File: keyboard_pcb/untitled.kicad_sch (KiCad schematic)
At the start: 33 parts, among them J1 USB_C_Receptacle_USB2.0_16P, J2 Conn_01x02, SW1 Reset, U1 RP2040, U2 NCP1117-3.3_SOT223, U3 W25Q128JVS, Y1 Crystal_GND24

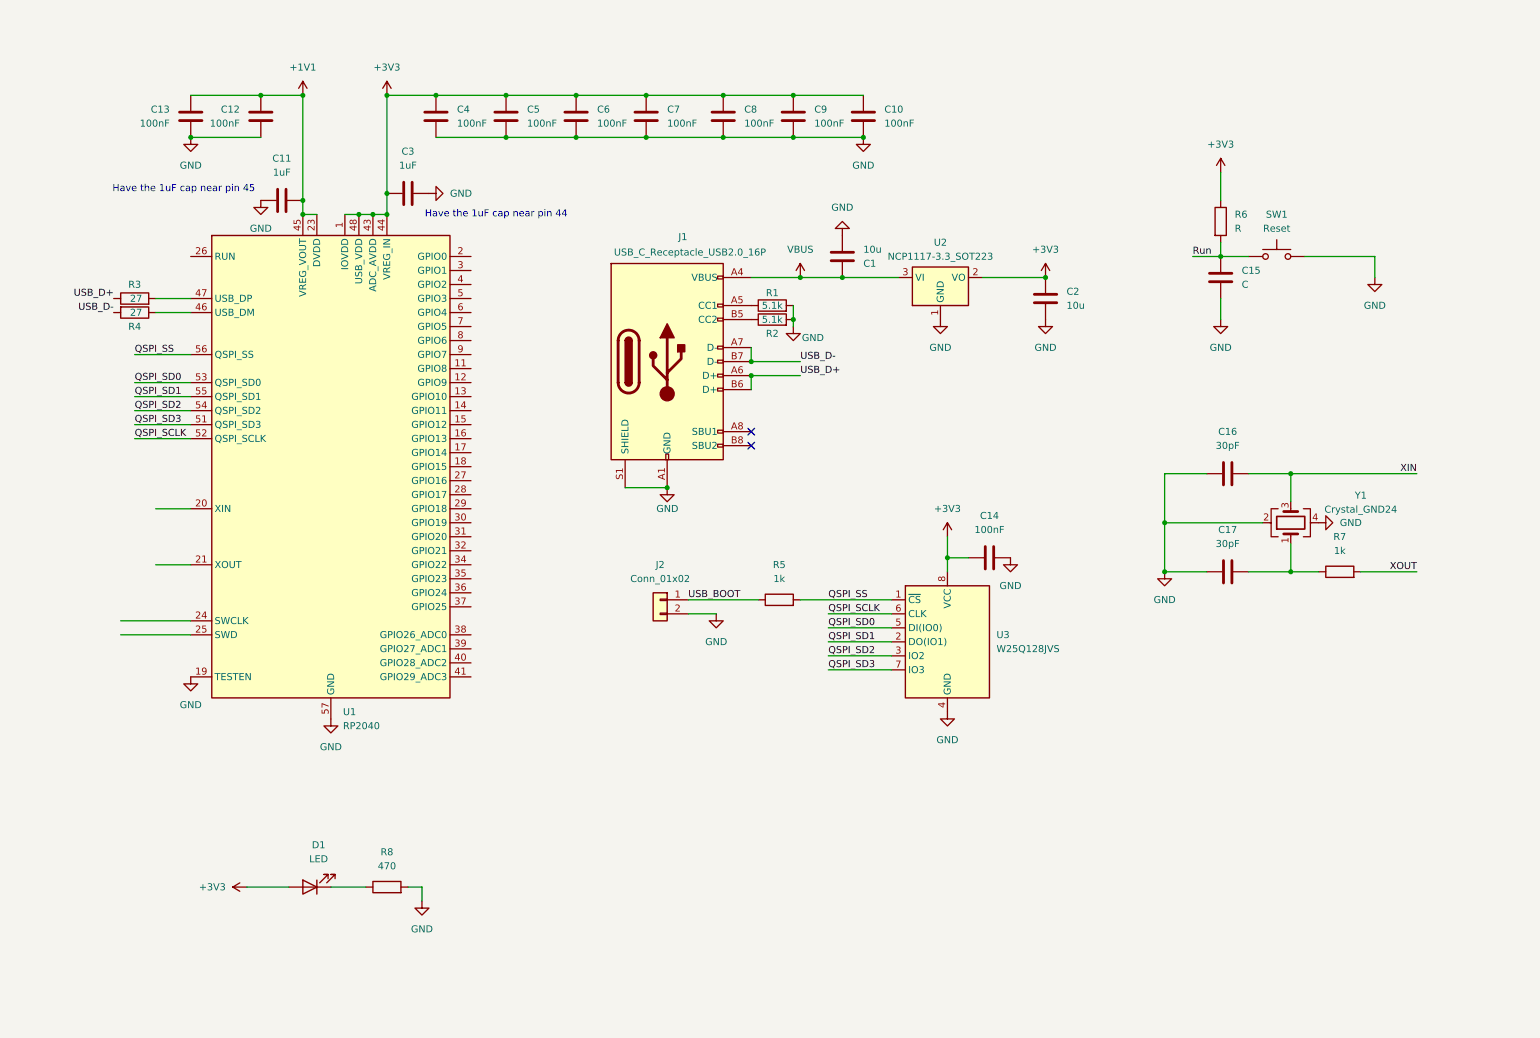
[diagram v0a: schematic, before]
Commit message: implemented matrix
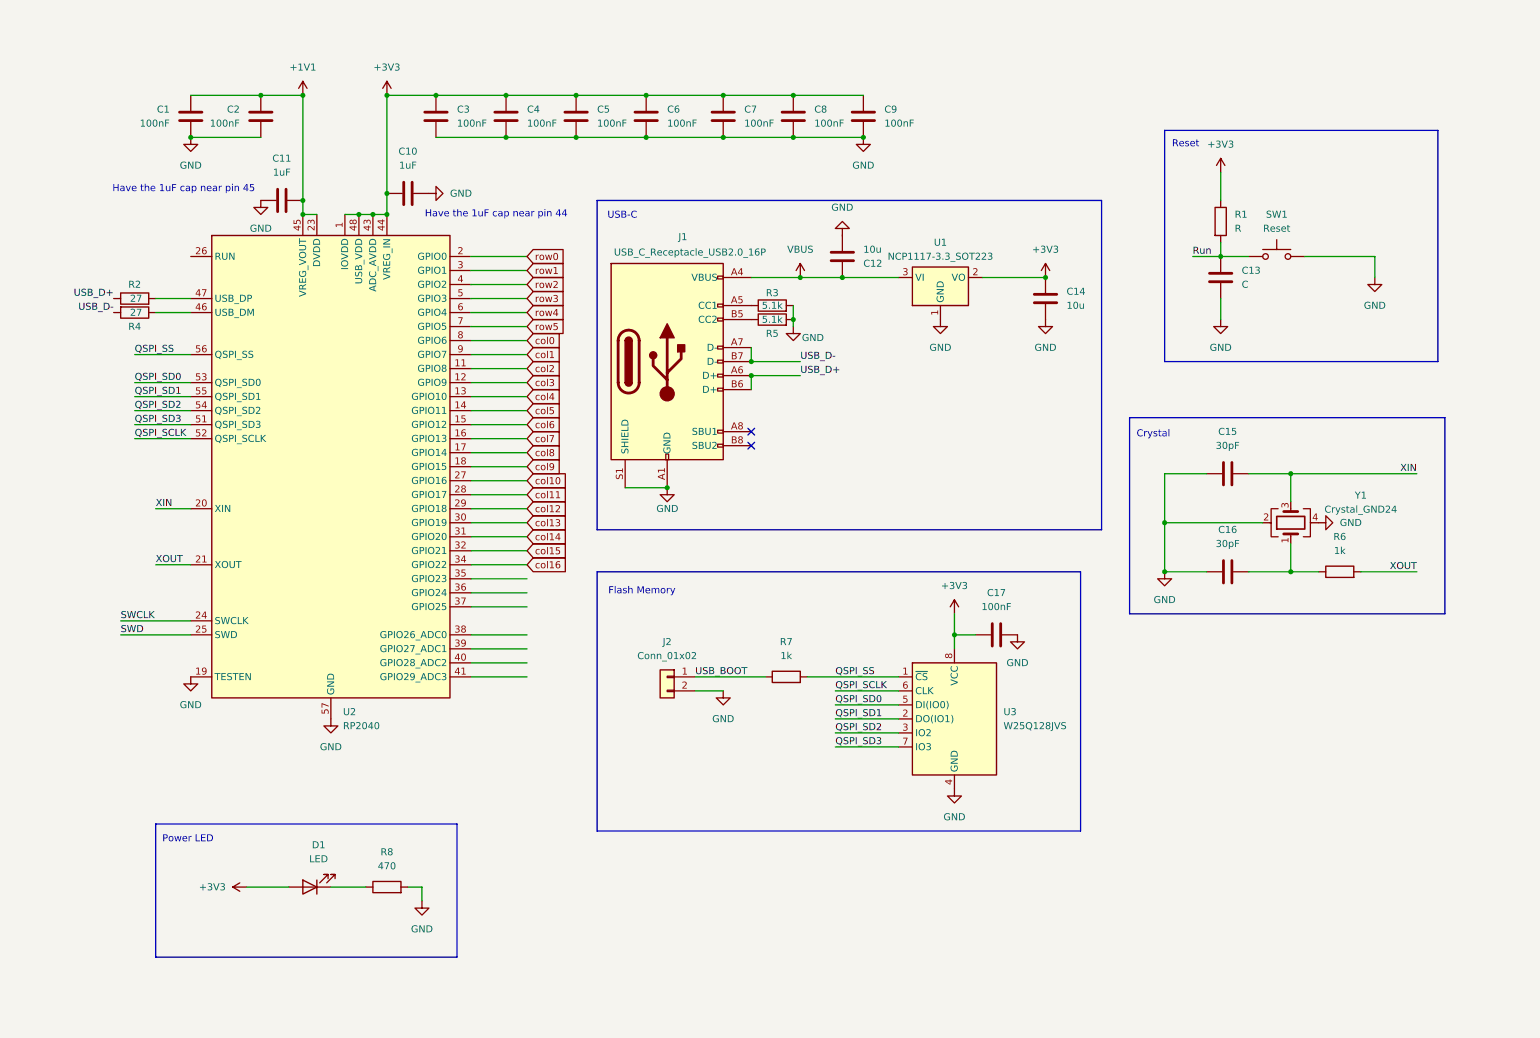
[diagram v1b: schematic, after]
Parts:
- renumbered C13 to C1, C3 to C10, C1 to C12, C15 to C13, C2 to C14, C16 to C15, C17 to C16, C14 to C17, C12 to C2, C4 to C3, C5 to C4, C6 to C5, C7 to C6, C8 to C7, C9 to C8, C10 to C9, R6 to R1, R3 to R2, R1 to R3, R2 to R5, R7 to R6, R5 to R7, U2 to U1, U1 to U2
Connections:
- net XIN: now also U2.20 (XIN)
- net XOUT: now also U2.21 (XOUT)
- net col2: now reaches U2.11 (GPIO8)
- net col3: now reaches U2.12 (GPIO9)
- net col4: now reaches U2.13 (GPIO10)
- net col5: now reaches U2.14 (GPIO11)
- net col6: now reaches U2.15 (GPIO12)
- net col7: now reaches U2.16 (GPIO13)
- net col8: now reaches U2.17 (GPIO14)
- net col9: now reaches U2.18 (GPIO15)
- net row0: now reaches U2.2 (GPIO0)
- net SWCLK: now reaches U2.24 (SWCLK)
- net SWD: now reaches U2.25 (SWD)
- net col10: now reaches U2.27 (GPIO16)
- net col11: now reaches U2.28 (GPIO17)
- net col12: now reaches U2.29 (GPIO18)
- net row1: now reaches U2.3 (GPIO1)
- net col13: now reaches U2.30 (GPIO19)
- net col14: now reaches U2.31 (GPIO20)
- net col15: now reaches U2.32 (GPIO21)
- net col16: now reaches U2.34 (GPIO22)
- net row2: now reaches U2.4 (GPIO2)
- net row3: now reaches U2.5 (GPIO3)
- net row4: now reaches U2.6 (GPIO4)
- net row5: now reaches U2.7 (GPIO5)
- net col0: now reaches U2.8 (GPIO6)
- net col1: now reaches U2.9 (GPIO7)
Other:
- note added: "Crystal"
- note added: "Flash Memory"
- note added: "Power LED"
- note added: "Reset"
- note added: "USB-C"
- moved on the sheet: C17, J2, R7, U3

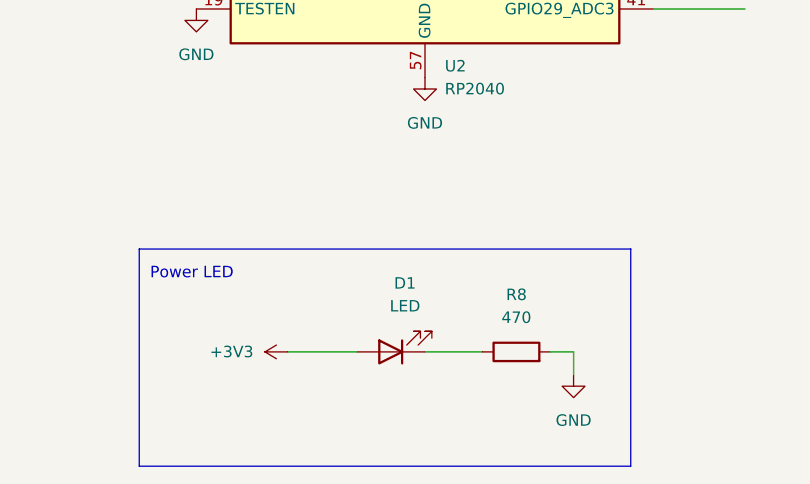
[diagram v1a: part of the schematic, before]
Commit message: implemented LEDs and switch and diode layout
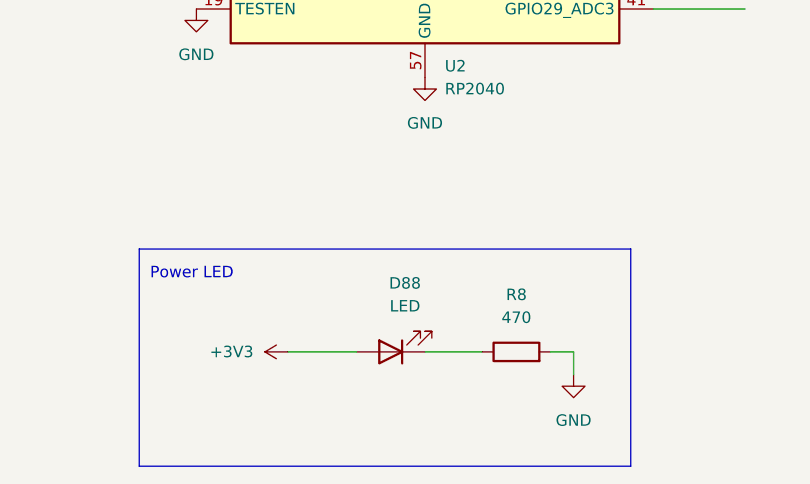
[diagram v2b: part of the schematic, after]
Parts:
- renumbered D1 to D88
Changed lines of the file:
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@@
 		(dnp no)
 		(fields_autoplaced yes)
-		(property "Reference" "D1"
+		(property "Reference" "D88"
 			(at 65.0875 163.83 0)
 			(effects
@@
 			(project ""
 				(path "/5a0b976f-d314-4fca-8ab0-732ea8a514fc/1c1519bd-c066-477c-a904-4026770e74a9"
-					(reference "D1")
+					(reference "D88")
 					(unit 1)
 				)

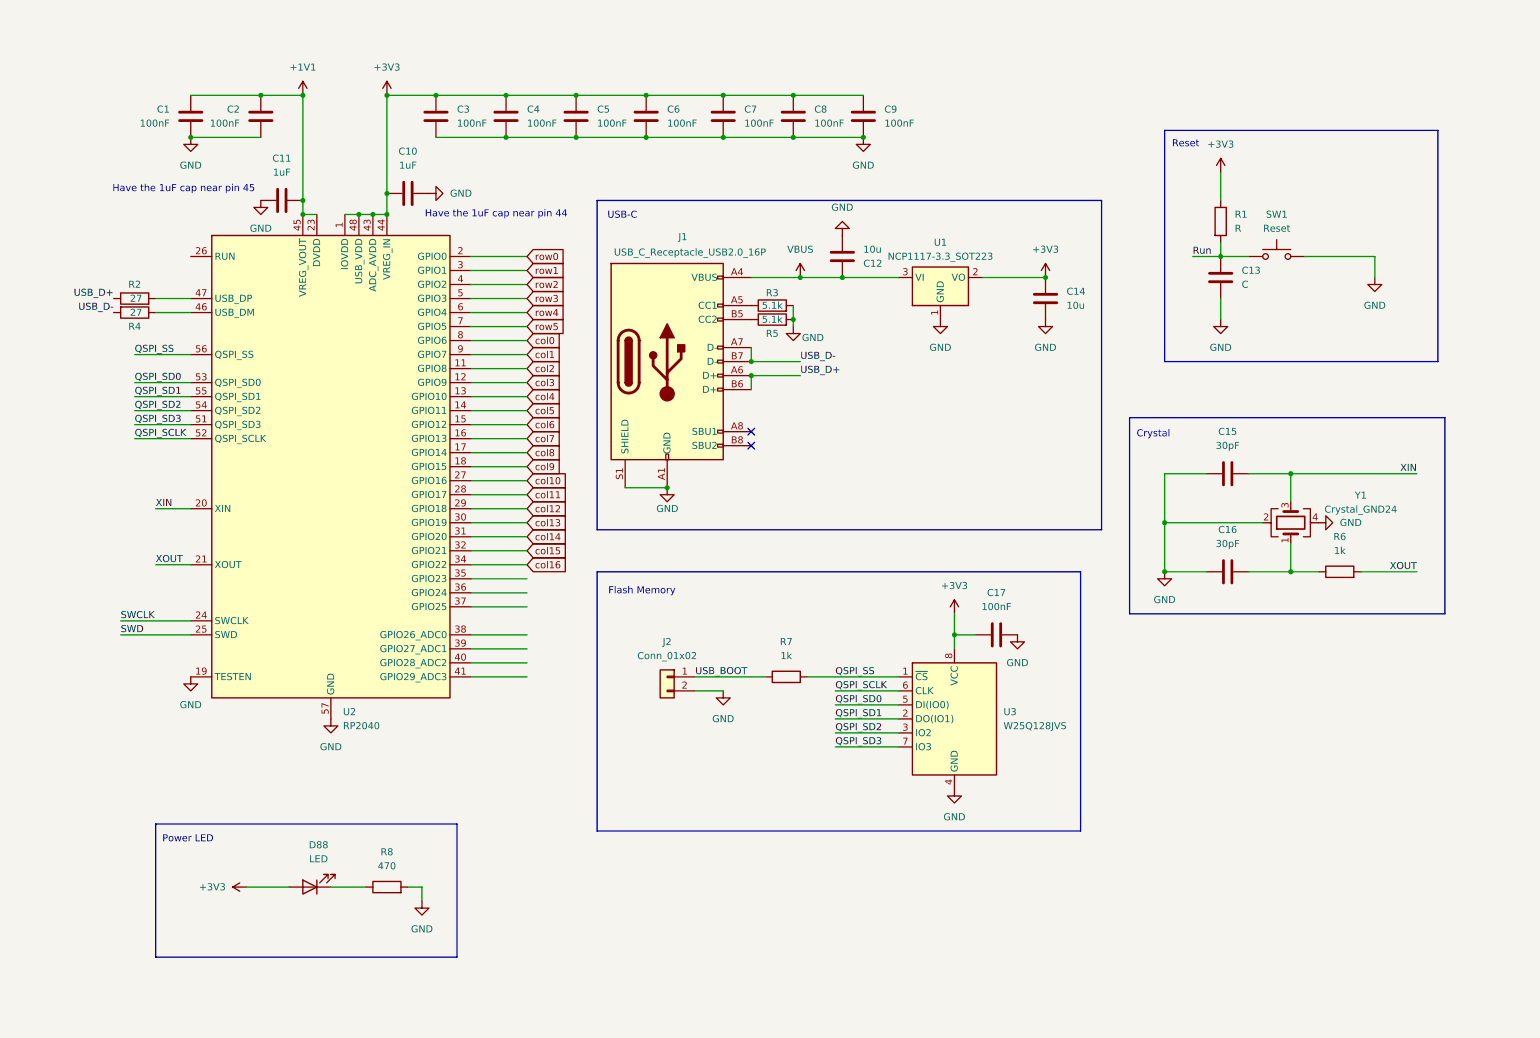
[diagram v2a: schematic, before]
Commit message: added led capacitors and route all leds
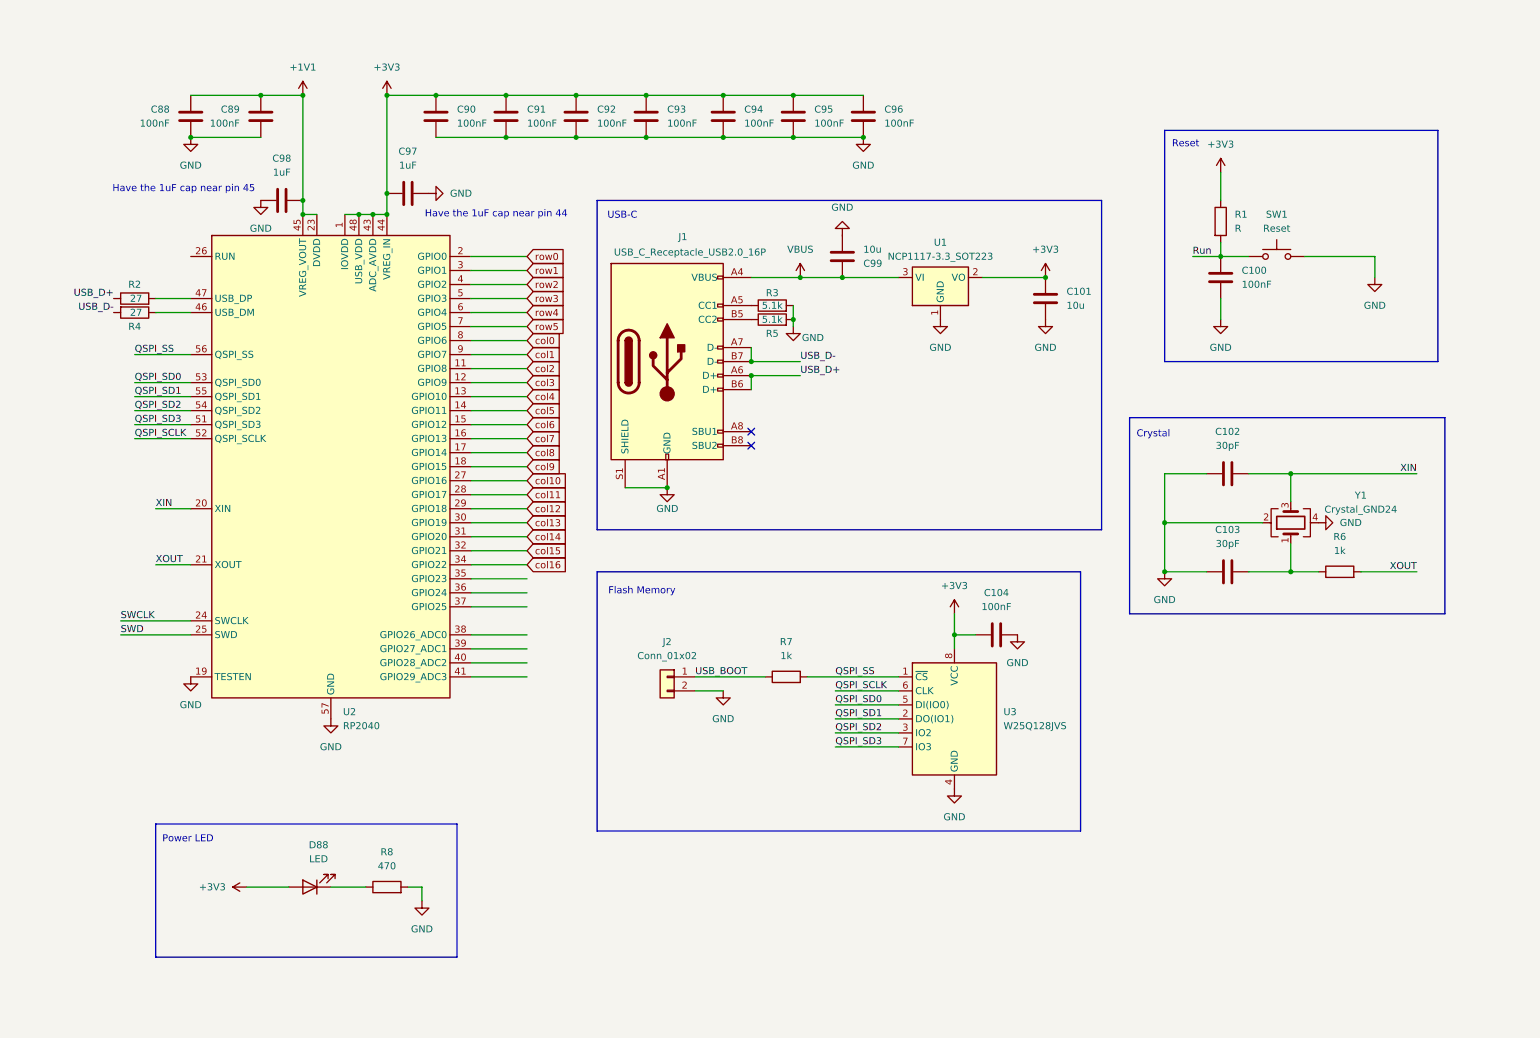
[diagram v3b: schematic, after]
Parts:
- C100: renamed from C13; value C -> 100nF; footprint (none) -> Capacitor_SMD:C_0603_1608Metric_Pad1.08x0.95mm_HandSolder
- C101: renamed from C14; footprint (none) -> Capacitor_SMD:C_0603_1608Metric_Pad1.08x0.95mm_HandSolder
- C102: renamed from C15; footprint (none) -> Capacitor_SMD:C_0603_1608Metric_Pad1.08x0.95mm_HandSolder
- C103: renamed from C16; footprint (none) -> Capacitor_SMD:C_0603_1608Metric_Pad1.08x0.95mm_HandSolder
- C104: renamed from C17; footprint (none) -> Capacitor_SMD:C_0603_1608Metric_Pad1.08x0.95mm_HandSolder
- C88: renamed from C1; footprint (none) -> Capacitor_SMD:C_0603_1608Metric_Pad1.08x0.95mm_HandSolder
- C89: renamed from C2; footprint (none) -> Capacitor_SMD:C_0603_1608Metric_Pad1.08x0.95mm_HandSolder
- C90: renamed from C3; footprint (none) -> Capacitor_SMD:C_0603_1608Metric_Pad1.08x0.95mm_HandSolder
- C91: renamed from C4; footprint (none) -> Capacitor_SMD:C_0603_1608Metric_Pad1.08x0.95mm_HandSolder
- C92: renamed from C5; footprint (none) -> Capacitor_SMD:C_0603_1608Metric_Pad1.08x0.95mm_HandSolder
- C93: renamed from C6; footprint (none) -> Capacitor_SMD:C_0603_1608Metric_Pad1.08x0.95mm_HandSolder
- C94: renamed from C7; footprint (none) -> Capacitor_SMD:C_0603_1608Metric_Pad1.08x0.95mm_HandSolder
- C95: renamed from C8; footprint (none) -> Capacitor_SMD:C_0603_1608Metric_Pad1.08x0.95mm_HandSolder
- C96: renamed from C9; footprint (none) -> Capacitor_SMD:C_0603_1608Metric_Pad1.08x0.95mm_HandSolder
- C97: renamed from C10; footprint (none) -> Capacitor_SMD:C_0603_1608Metric_Pad1.08x0.95mm_HandSolder
- C98: renamed from C11; footprint (none) -> Capacitor_SMD:C_0603_1608Metric_Pad1.08x0.95mm_HandSolder
- C99: renamed from C12; footprint (none) -> Capacitor_SMD:C_0603_1608Metric_Pad1.08x0.95mm_HandSolder

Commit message: updated schematic
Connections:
- net +1V1: no longer U2.23 (DVDD), U2.45 (VREG_VOUT), U2.50 (DVDD)
- net +3V3: no longer U2.1 (IOVDD), U2.10 (IOVDD), U2.22 (IOVDD), U2.33 (IOVDD), U2.42 (IOVDD), U2.43 (ADC_AVDD), U2.44 (VREG_IN), U2.48 (USB_VDD), U2.49 (IOVDD)
- new net: U2.1 (IOVDD), U2.10 (IOVDD), U2.22 (IOVDD), U2.33 (IOVDD), U2.42 (IOVDD), U2.43 (ADC_AVDD), U2.44 (VREG_IN), U2.48 (USB_VDD), U2.49 (IOVDD)
- new net: U2.23 (DVDD), U2.45 (VREG_VOUT), U2.50 (DVDD)
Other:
- note added: "Decoupling Capacitor"
- note added: "MCU (RP2040)"
- moved on the sheet: C100, C101, C102, C103, C104, C88, C89, C90, C91, C92, C93, C94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
